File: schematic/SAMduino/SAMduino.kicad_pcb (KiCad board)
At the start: 4 copper layers, 100 x 100 mm, 97 parts, among them IC1 ATSAMV71N21B-AABT, IC2 MCP1703AT-5002E_CB, IC3 NCP5501DT33RKG, IC4 SST26VF064B-104V_SM, IC5 MCP2221-I_SL, IC6 MCP2542FD-E_SN, J1 Barrel_Jack_Switch, J10 Conn_02x11_Odd_Even, J11 Conn_02x09_Odd_Even, J12 Conn_02x09_Odd_Even, J13 Conn_01x02, J14 Conn_02x02_Odd_Even, J15 Conn_02x03_Odd_Even, J16 Conn_01x02, J17 Conn_02x03_Odd_Even, J18 Conn_02x02_Odd_Even, J19 Conn_02x03_Odd_Even, J2 Conn_02x02_Odd_Even, J20 Conn_01x08, J3 USB_B_Micro, J4 USB_B_Mini, J5 Conn_01x02, J6 Screw_Terminal_01x02, J7 Conn_01x02, J8 Conn_01x02, J9 Conn_02x07_Odd_Even, SW1 SW_MEC_5E, SW2 SW_MEC_5E, SW3 MCLR, SW4 ERASE, X1 12 MHz, X2 32.768 kHz 12.5 pF

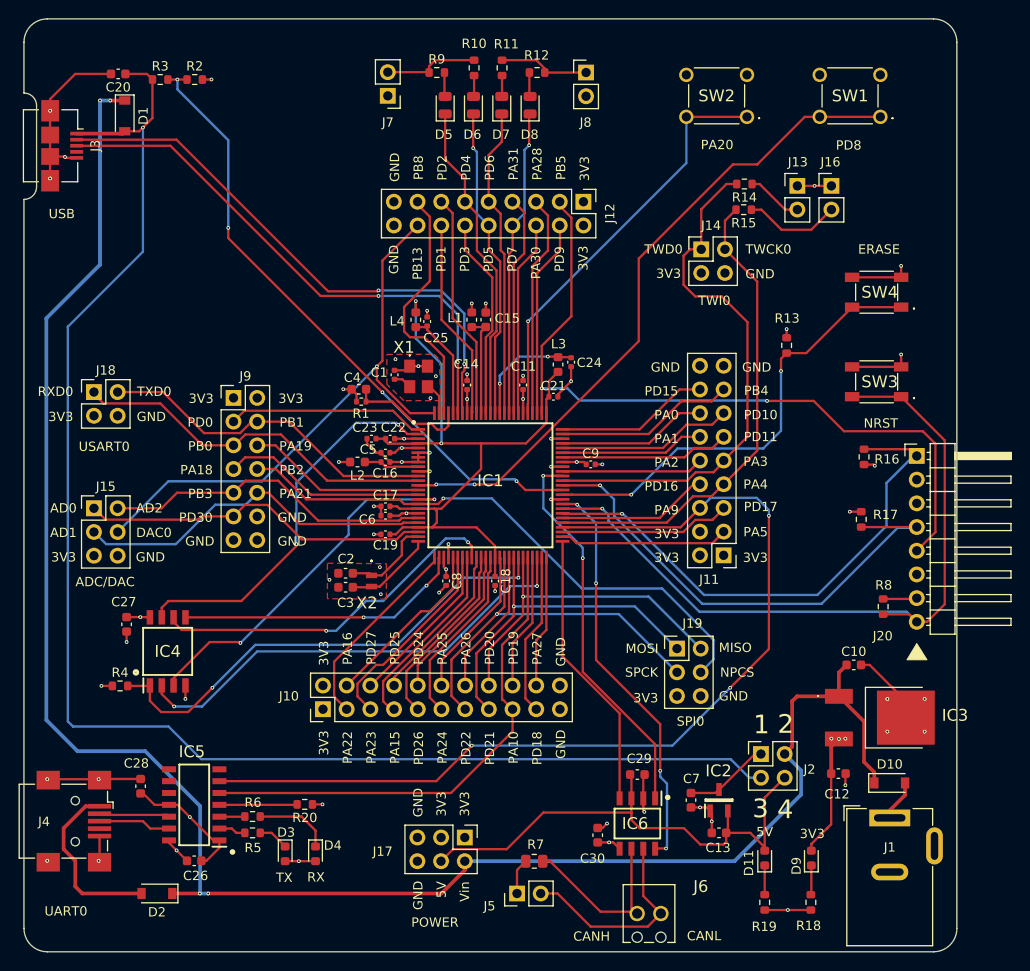
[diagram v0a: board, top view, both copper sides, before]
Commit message: Changed voltage regulators
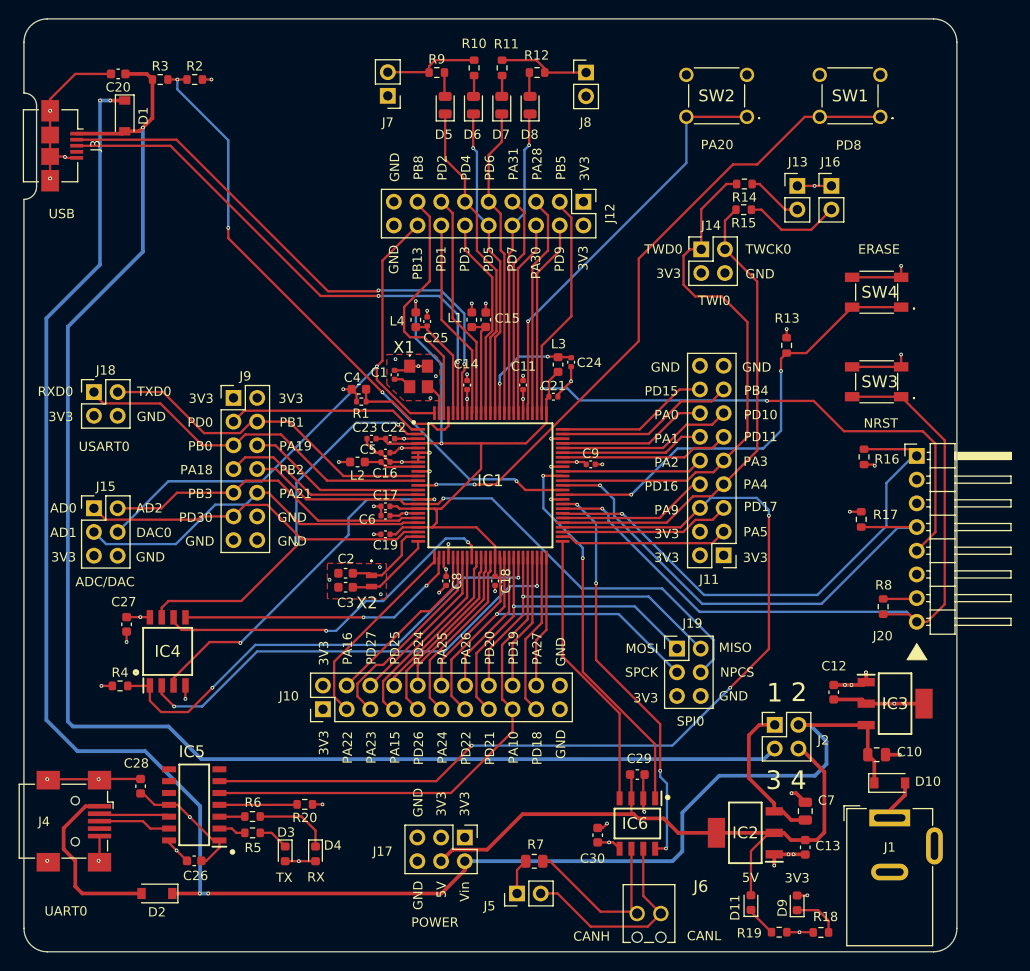
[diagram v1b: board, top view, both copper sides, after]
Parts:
- C10: value 10uF -> 22uF; footprint Capacitor_SMD:C_0603_1608Metric -> Capacitor_SMD:C_0805_2012Metric
- C12: value 4.7uF -> 22uF
- C13: value 1uF -> 22uF
- C7: value 1uF -> 22uF; footprint Capacitor_SMD:C_0603_1608Metric -> Capacitor_SMD:C_0805_2012Metric
- IC2: value MCP1703AT-5002E_CB -> AZ1117CH-5.0TRG1; footprint SamacSys_Parts:SOT95P255X145-3N -> SamacSys_Parts:SOT230P700X180-4N
- IC3: value NCP5501DT33RKG -> AZ1117IH-3.3TRG1; footprint SamacSys_Parts:NVD5117PLT4GVF01 -> SamacSys_Parts:SOT230P700X180-4N
- moved C7 12.3 mm to (117.0, 136.2), turned to 90 degrees
- moved C10 9.93 mm to (124.7, 130.1)
- moved C13 9.38 mm to (117.0, 140.1), turned to 270 degrees
- moved C12 8.74 mm to (120.0, 123.4), turned to 90 degrees
- moved D9 5.04 mm to (116.1, 146.0)
- moved D11 5.00 mm to (111.2, 146.0)
- moved IC2 4.50 mm to (110.6, 138.5), turned to 180 degrees
- moved R19 3.56 mm to (114.2, 149.2), turned to 0 degrees
- moved J2 3.46 mm to (113.7, 126.9)
- moved R18 3.40 mm to (118.7, 149.2), turned to 180 degrees
- moved IC3 3.29 mm to (126.6, 124.7), turned to 0 degrees
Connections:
- IC3 pad 1: VIN -> GND
- IC3 pad 2: GND -> VCC3V3
- IC3 pad 3: VCC3V3 -> VIN
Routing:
- net VDD5V: track 56.7 -> 67.3 mm
- net Net-(C7-Pad1): track 9.23 -> 16.2 mm
- net GND: track 108.5 -> 102.7 mm, vias 49 -> 50
- net VIN: track 204.3 -> 200.0 mm
- net VCC3V3: track 76.1 -> 73.7 mm, vias 22 -> 23
- net Net-(D9-Pad1): track 3.49 -> 5.10 mm
- net VUSB5V: track 159.9 -> 161.0 mm
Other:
- board text added: "ATSAMV71N21B"

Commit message: Removed D10
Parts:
- removed D10: MBR0520LT, Diode_SMD:D_SOD-123
- C10, C7: value 22uF -> 10uF
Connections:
- J1 pad 1: Net-(D10-Pad2) -> VIN
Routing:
- net VIN: track 200.0 -> 205.2 mm
- net Net-(D10-Pad2): track 4.43 -> 0.00 mm
- net GND: track 102.7 -> 103.6 mm, vias 50 -> 51
- net VCC3V3: vias 23 -> 24

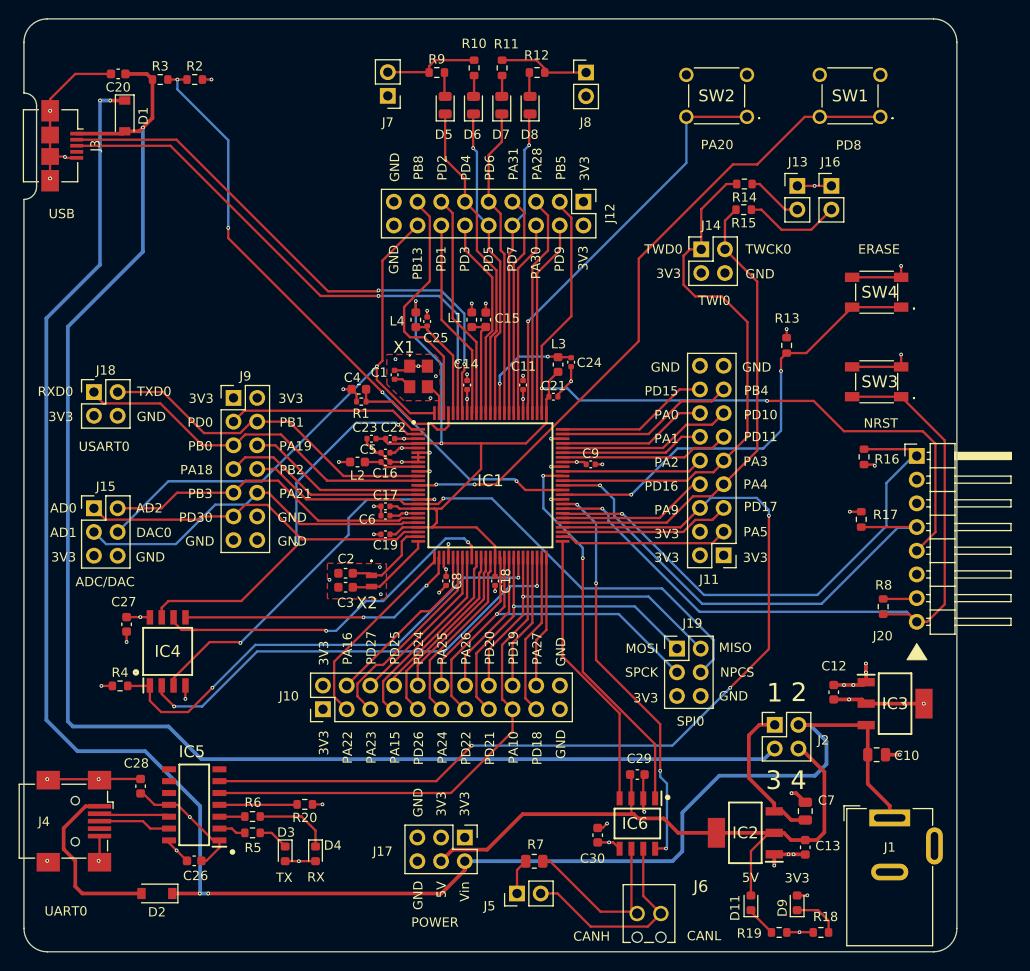
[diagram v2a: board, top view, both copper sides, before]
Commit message: Changed via size
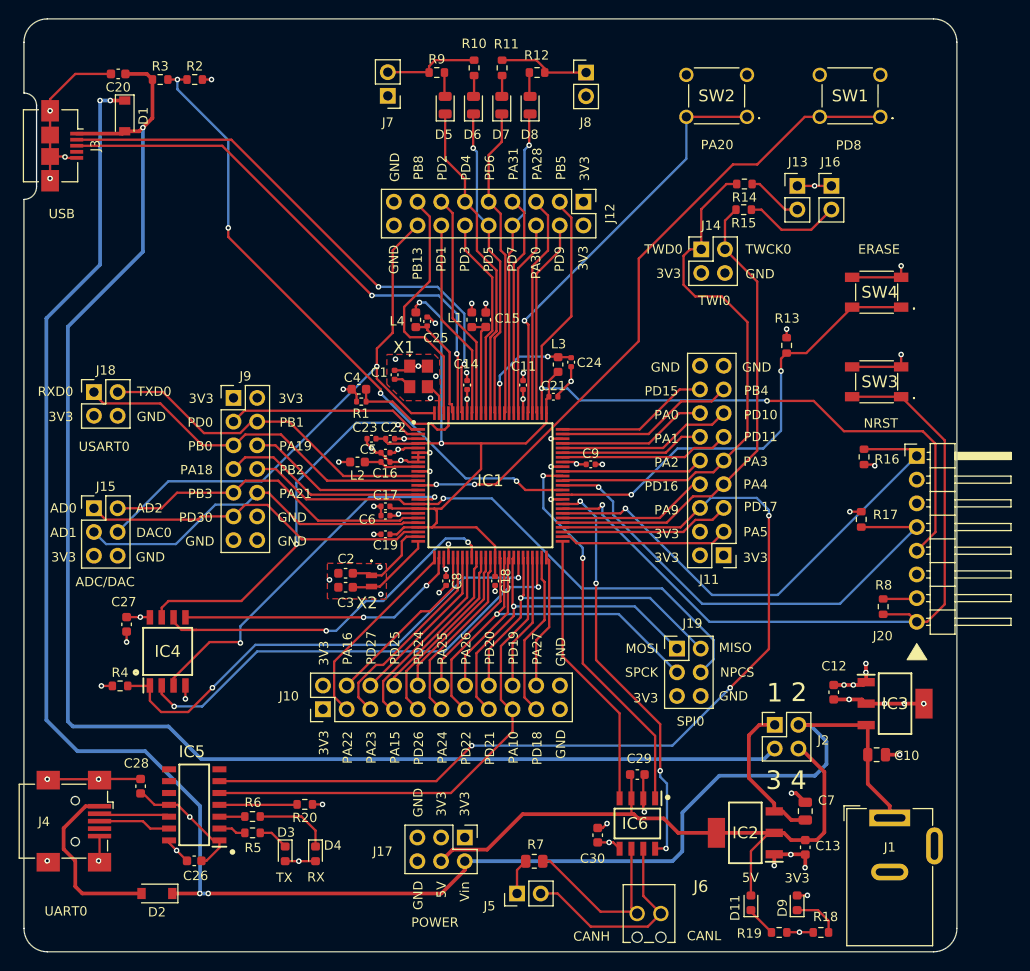
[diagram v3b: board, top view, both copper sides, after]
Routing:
- net GND: track 103.6 -> 106.1 mm
- net SWDIO: track 57.4 -> 55.1 mm
- net CAN_STBY: track 43.7 -> 44.3 mm
- net NRST: track 80.5 -> 81.1 mm
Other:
- net class Default: via_dia 0.4 -> 0.6; via_drill 0.2 -> 0.3
- net class Power: via_dia 0.4 -> 0.6; via_drill 0.2 -> 0.3
- rule trace_min: 0.1 -> 0.25
- rule via_min_size: 0.4 -> 0.6
